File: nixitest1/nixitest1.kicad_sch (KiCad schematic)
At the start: 27 parts

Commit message: Add flyback.
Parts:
- removed T?: 1:10, symbol Device:Transformer_1P_1S
- added T1: Flyback-ATB3225, Flyback-ATB3225:Flyback-ATB3225, symbol Flyback-ATB3225:Flyback-ATB3225
- NE1, NE2: renamed from NE?; footprint (none) -> neonglow:neonglow
- gave numbers to parts that had none: 24
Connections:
- net +5V: now also T1.1
- net GND: now also T1.2
- net at Q1.3 (D): now also T1.4
- net at D1.2 (A): now also T1.3
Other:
- moved on the sheet: C1, D1, Q1, R1, R2, R3, R4

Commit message: Update design.
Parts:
- removed R5: 18kΩ 1206 1% 250mW, Resistor_SMD:R_1206_3216Metric, symbol Device:R
- added C2: 10uF 25V, Capacitor_SMD:C_0603_1608Metric, symbol Device:C
- added C3: 100n, Capacitor_SMD:C_0402_1005Metric, symbol Device:C
- added J1: MSYS, Connector_PinHeader_2.54mm:PinHeader_2x05_P2.54mm_Horizontal, symbol Connector_Generic:Conn_02x05_Odd_Even
- added J2, J3, J4: ~, rawpad22:rawpad22, symbol Connector_Generic:Conn_01x01
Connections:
- net +5V: now also C2.1, C3.1, J1.5 (Pin_5), J1.6 (Pin_6)
- net ANODE: now also NE1.1, NE2.1
- net GND: now also C2.2, C3.2, J1.1 (Pin_1), J1.10 (Pin_10), J1.2 (Pin_2), J1.9 (Pin_9), J2.1 (Pin_1), J3.1 (Pin_1), J4.1 (Pin_1)
- net PGM: now reaches U1.15 (PD1/SWIO/AETR/T1CH3/SCL/URX)
- net PGM: now also J1.3 (Pin_3), J1.8 (Pin_8)
- net URX: now reaches U1.19 (PD5/A5/UTX/T2CH4/URX)
- net URX: now also J1.4 (Pin_4)
- net UTX: now reaches U1.20 (PD6/A7/URX/T2CH3/UTX)
- net UTX: now also J1.7 (Pin_7)

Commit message: Ok actually ready for production.
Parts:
- R1: value 300mΩ -> 500mΩ; footprint Resistor_SMD:R_1206_3216Metric -> Resistor_SMD:R_0805_2012Metric; LCSC C2907398 -> C327217
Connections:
- net +5V: now also J3.1 (Pin_1)
- net DIG_AUX: now also U1.1 (PD7/NRST/T2CH4/OPP1/UCK); no longer U1.2 (PA1/OSCI/A1/T1CH2/OPN0)
- net GND: no longer J3.1 (Pin_1), J4.1 (Pin_1)
- net HVCTL: now also U1.2 (PA1/OSCI/A1/T1CH2/OPN0); no longer U1.1 (PD7/NRST/T2CH4/OPP1/UCK)
- net PGM: now also J4.1 (Pin_1)
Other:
- moved on the sheet: D1, R6, R7

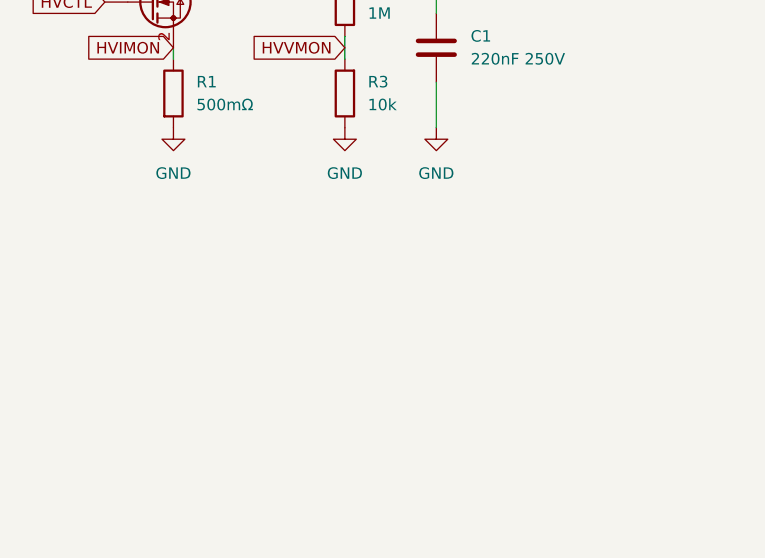
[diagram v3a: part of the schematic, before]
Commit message: Update comments on nixietest + Add debug tool. + Add ch32v003 firmware for the controller.
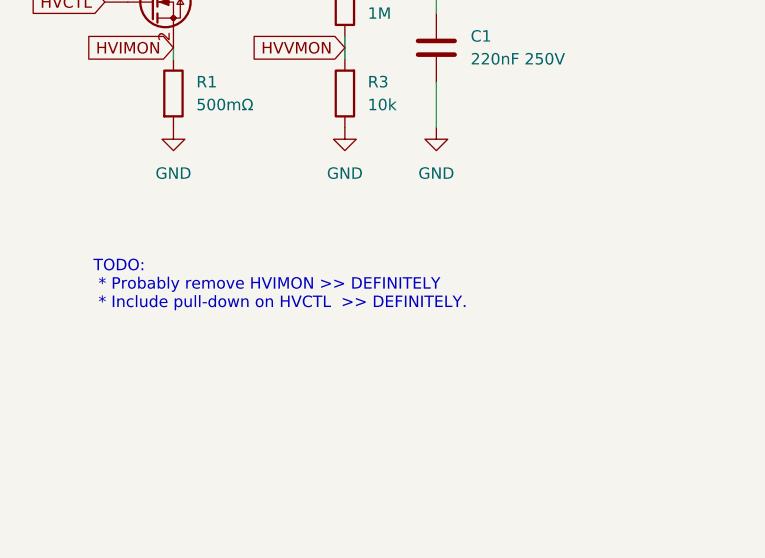
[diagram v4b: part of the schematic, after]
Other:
- note added: "TODO: * Probably remove HVIMON >> DEFINITELY * Include pull-down on HVCTL >> DEFINITELY."
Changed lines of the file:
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@@
+    (effects (font (size 1.27 1.27)) (justify left bottom))
+  )
+  (text "TODO:\n * Probably remove HVIMON >> DEFINITELY\n * Include pull-down on HVCTL  >> DEFINITELY.\n"
+    (at 24.13 147.32 0)
     (effects (font (size 1.27 1.27)) (justify left bottom))
   )

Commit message: Update board design
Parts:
- R1: value 500mΩ -> 10k; footprint Resistor_SMD:R_0805_2012Metric -> Resistor_SMD:R_0402_1005Metric; LCSC C327217 -> C25744
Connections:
- net GND: now also Q1.2 (S), R1.1; no longer R1.2
- net HVCTL: now also R1.2
- removed net HVIMON: Q1.2 (S), R1.1, U1.3 (PA2/OSCO/A0/T1CH2N/OPP0/AETR2)
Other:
- note added: "Changes in RevA * Probably remove HVIMON >> DEFINITELY * Include pull-down on HVCTL >> DEFINITELY. * Monitor ripple on HVP Mod per Ivan."
- note removed: "TODO: * Probably remove HVIMON >> DEFINITELY * Include pull-down on HVCTL >> DEFINITELY."
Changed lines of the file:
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@@
   (junction (at 116.84 113.03) (diameter 0) (color 0 0 0 0)
   )
+  (junction (at 33.02 124.46) (diameter 0) (color 0 0 0 0)
+  )
   (junction (at 52.07 107.95) (diameter 0) (color 0 0 0 0)
   )
+  (wire (pts (xy 25.4 113.03) (xy 25.4 116.84))
+    (stroke (width 0) (type default) (color 0 0 0 0))
+  )
   (wire (pts (xy 52.07 109.22) (xy 52.07 107.95))
     (stroke (width 0) (type default) (color 0 0 0 0))
@@
     (stroke (width 0) (type default) (color 0 0 0 0))
   )
-  (wire (pts (xy 33.02 119.38) (xy 33.02 118.11))
+  (wire (pts (xy 33.02 118.11) (xy 33.02 124.46))
     (stroke (width 0) (type default) (color 0 0 0 0))
   )
   (wire (pts (xy 62.23 121.92) (xy 62.23 127))
+    (stroke (width 0) (type default) (color 0 0 0 0))
+  )
+  (wire (pts (xy 25.4 124.46) (xy 33.02 124.46))
     (stroke (width 0) (type default) (color 0 0 0 0))
   )
@@
     (effects (font (size 1.27 1.27)) (justify left bottom))
   )
-  (text "TODO:\n * Probably remove HVIMON >> DEFINITELY\n * Include pull-down on HVCTL  >> DEFINITELY.\n"
+  (text "Changes in RevA\n * Probably remove HVIMON >> DEFINITELY\n * Include pull-down on HVCTL  >> DEFINITELY.\n * Monitor ripple on HVP\n\nMod per Ivan."
     (at 24.13 147.32 0)
     (effects (font (size 1.27 1.27)) (justify left bottom))
@@
     )
   )
-  (global_label "HVIMON" (shape input) (at 31.75 39.37 180) (fields_autoplaced)
-    (effects (font (size 1.27 1.27)) (justify right))
-    (property "Intersheet References" "${INTERSHEET_REFS}" (id 0) (at 22.2007 39.2906 0)
-      (effects (font (size 1.27 1.27)) (justify right) hide)
-    )
-  )
   (global_label "DIG_DOT" (shape input) (at 234.95 104.14 180) (fields_autoplaced)
     (effects (font (size 1.27 1.27)) (justify right))
@@
     (effects (font (size 1.27 1.27)) (justify right))
     (property "Intersheet References" "${INTERSHEET_REFS}" (id 0) (at 234.2907 59.6106 0)
-      (effects (font (size 1.27 1.27)) (justify right) hide)
-    )
-  )
-  (global_label "HVIMON" (shape input) (at 33.02 118.11 180) (fields_autoplaced)
-    (effects (font (size 1.27 1.27)) (justify right))
-    (property "Intersheet References" "${INTERSHEET_REFS}" (id 0) (at 23.4707 118.0306 0)
       (effects (font (size 1.27 1.27)) (justify right) hide)
     )
@@
     (pin "9")
   )
+  (symbol (lib_id "Device:R") (at 25.4 120.65 180) (unit 1)
+    (in_bom yes) (on_board yes) (fields_autoplaced)
+    (property "Reference" "R1" (id 0) (at 27.94 119.3799 0)
+      (effects (font (size 1.27 1.27)) (justify right))
+    )
+    (property "Value" "10k" (id 1) (at 27.94 121.9199 0)
+      (effects (font (size 1.27 1.27)) (justify right))
+    )
+    (property "Footprint" "Resistor_SMD:R_0402_1005Metric" (id 2) (at 27.178 120.65 90)
+      (effects (font (size 1.27 1.27)) hide)
+    )
+    (property "Datasheet" "~" (id 3) (at 25.4 120.65 0)
+      (effects (font (size 1.27 1.27)) hide)
+    )
+    (property "LCSC" "C25744" (id 4) (at 25.4 120.65 90)
+      (effects (font (size 1.27 1.27)) hide)
+    )
+    (pin "1")
+    (pin "2")
+  )
   (symbol (lib_id "Device:R") (at 52.07 113.03 180) (unit 1)
     (in_bom yes) (on_board yes) (fields_autoplaced)
@@
   (symbol (lib_id "power:+5V") (at 163.83 165.1 180) (unit 1)
     (in_bom yes) (on_board yes)
-    (property "Reference" "#PWR?" (id 0) (at 163.83 161.29 0)
+    (property "Reference" "#PWR0131" (id 0) (at 163.83 161.29 0)
       (effects (font (size 1.27 1.27)) hide)
     )
@@
     (pin "2")
     (pin "3")
-  )
-  (symbol (lib_id "Device:R") (at 33.02 123.19 0) (unit 1)
-    (in_bom yes) (on_board yes) (fields_autoplaced)
-    (property "Reference" "R1" (id 0) (at 35.56 121.9199 0)
-      (effects (font (size 1.27 1.27)) (justify left))
-    )
-    (property "Value" "500mΩ" (id 1) (at 35.56 124.4599 0)
-      (effects (font (size 1.27 1.27)) (justify left))
-    )
-    (property "Footprint" "Resistor_SMD:R_0805_2012Metric" (id 2) (at 31.242 123.19 90)
-      (effects (font (size 1.27 1.27)) hide)
-    )
-    (property "Datasheet" "~" (id 3) (at 33.02 123.19 0)
-      (effects (font (size 1.27 1.27)) hide)
-    )
-    (property "LCSC" "C327217" (id 4) (at 33.02 123.19 0)
-      (effects (font (size 1.27 1.27)) hide)
-    )
-    (pin "1")
-    (pin "2")
   )
   (symbol (lib_id "power:GND") (at 120.65 152.4 90) (unit 1)
@@
     (pin "1")
   )
-  (symbol (lib_id "power:GND") (at 33.02 127 0) (unit 1)
-    (in_bom yes) (on_board yes) (fields_autoplaced)
-    (property "Reference" "#PWR0105" (id 0) (at 33.02 133.35 0)
-      (effects (font (size 1.27 1.27)) hide)
-    )
-    (property "Value" "GND" (id 1) (at 33.02 132.08 0))
-    (property "Footprint" "" (id 2) (at 33.02 127 0)
-      (effects (font (size 1.27 1.27)) hide)
-    )
-    (property "Datasheet" "" (id 3) (at 33.02 127 0)
+  (symbol (lib_id "power:GND") (at 33.02 124.46 0) (unit 1)
+    (in_bom yes) (on_board yes) (fields_autoplaced)
+    (property "Reference" "#PWR0105" (id 0) (at 33.02 130.81 0)
+      (effects (font (size 1.27 1.27)) hide)
+    )
+    (property "Value" "GND" (id 1) (at 33.02 129.54 0))
+    (property "Footprint" "" (id 2) (at 33.02 124.46 0)
+      (effects (font (size 1.27 1.27)) hide)
+    )
+    (property "Datasheet" "" (id 3) (at 33.02 124.46 0)
       (effects (font (size 1.27 1.27)) hide)
     )
@@
       (reference "#PWR0130") (unit 1) (value "+5V") (footprint "")
     )
+    (path "/89bc2a9a-0459-4374-90b7-e699bb20f381"
+      (reference "#PWR0131") (unit 1) (value "+5V") (footprint "")
+    )
     (path "/8e0259d4-bb9a-4043-8fcc-b83ca78b22de"
       (reference "#PWR0134") (unit 1) (value "GND") (footprint "")
     )
-    (path "/89bc2a9a-0459-4374-90b7-e699bb20f381"
-      (reference "#PWR?") (unit 1) (value "+5V") (footprint "")
-    )
     (path "/2482b284-20c0-4ecb-b135-d475161041a6"
       (reference "C1") (unit 1) (value "220nF 250V") (footprint "Capacitor_SMD:C_1210_3225Metric")
@@
       (reference "Q13") (unit 1) (value "HVN") (footprint "Package_TO_SOT_SMD:SOT-23")
     )
-    (path "/b849800a-20e5-42db-b326-c26a6d6b61f2"
-      (reference "R1") (unit 1) (value "500mΩ") (footprint "Resistor_SMD:R_0805_2012Metric")
+    (path "/691da4ab-50d4-4c76-af0a-7c17081a0dce"
+      (reference "R1") (unit 1) (value "10k") (footprint "Resistor_SMD:R_0402_1005Metric")
     )
     (path "/69f99f8d-2e9e-4591-8851-e3166a2dae3e"

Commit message: General update for all
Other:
- note added: "Changes in RevA * Probably remove HVIMON >> DEFINITELY * Include pull-down on HVCTL >> DEFINITELY. * Monitor ripple on HVP (NOT AN ISSUE) TODO: Mod HW per Ivan. * Ripple is TINY. Can use smaller output cap. 100nF? * Output reverse-V is baaad. Maybe add a diode & cap to inverse rail of flyback? * Keep P7 on DIG_AUX. * Shrink binding post holes. * Mark off which pin on header is PGM * Reduce power 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"
- note removed: "Changes in RevA * Probably remove HVIMON >> DEFINITELY * Include pull-down on HVCTL >> DEFINITELY. * Monitor ripple on HVP Mod per Ivan."
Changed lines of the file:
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@@
     (effects (font (size 1.27 1.27)) (justify left bottom))
   )
-  (text "Changes in RevA\n * Probably remove HVIMON >> DEFINITELY\n * Include pull-down on HVCTL  >> DEFINITELY.\n * Monitor ripple on HVP\n\nMod per Ivan."
-    (at 24.13 147.32 0)
+  (text "Changes in RevA\n * Probably remove HVIMON >> DEFINITELY\n * Include pull-down on HVCTL  >> DEFINITELY.\n * Monitor ripple on HVP  (NOT AN ISSUE)\n\nTODO:\nMod HW per Ivan.\n * Ripple is TINY.  Can use smaller output cap.  100nF?\n * Output reverse-V is baaad.  Maybe add a diode & cap to inverse rail of flyback?\n * Keep P7 on DIG_AUX.\n * Shrink binding post holes.\n * Mark off which pin on header is PGM\n * Reduce power to comma\n * Switch resistors to 15k"
+    (at 16.51 166.37 0)
     (effects (font (size 1.27 1.27)) (justify left bottom))
   )
